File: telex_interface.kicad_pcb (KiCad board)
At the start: 4 copper layers, 61 x 34.5 mm, 14 parts, among them J1 DB25_Female_MountingHoles, J2 Conn_01x08, U1 max3387

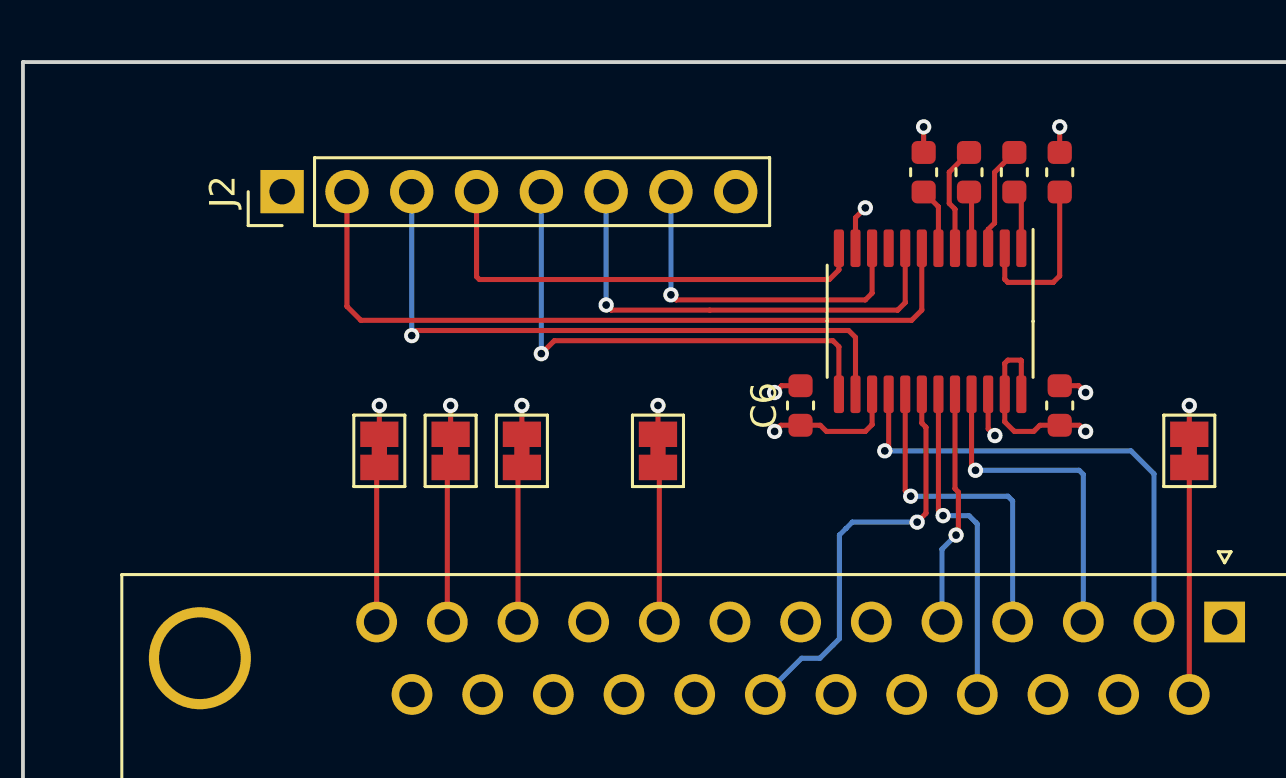
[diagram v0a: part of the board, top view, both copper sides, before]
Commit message: NAND gate for half dumplex echo and pullups
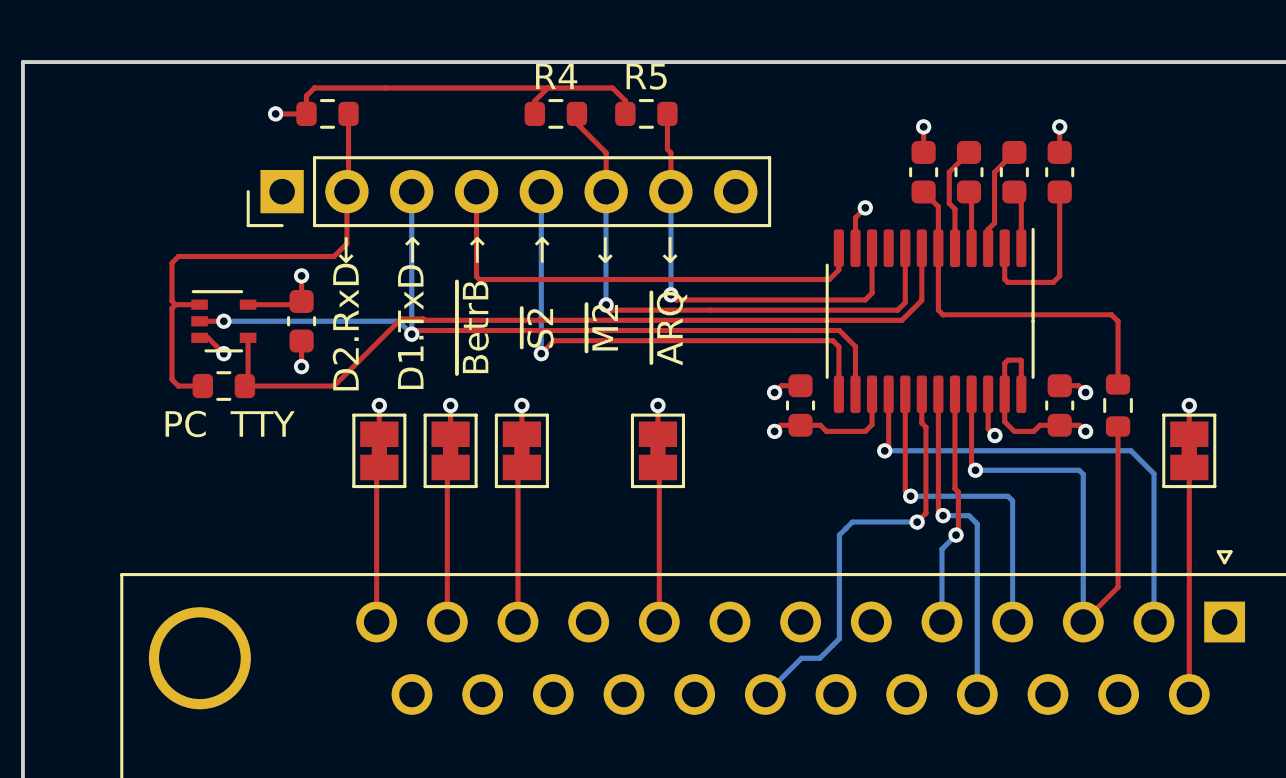
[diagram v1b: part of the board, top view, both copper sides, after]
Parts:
- added C7: 100n, Capacitor_SMD:C_0603_1608Metric, F.Cu at (158.2, 106.7)
- added R1: 3k6, Resistor_SMD:R_0603_1608Metric, F.Cu at (190.2, 110.0)
- added R2: 3k6, Resistor_SMD:R_0603_1608Metric, F.Cu at (159.3, 98.6)
- added R3: 0R (dnp), Resistor_SMD:R_0603_1608Metric, F.Cu at (155.2, 109.2)
- added R4: 3k6, Resistor_SMD:R_0603_1608Metric, F.Cu at (168.2, 98.6)
- added R5: 3k6, Resistor_SMD:R_0603_1608Metric, F.Cu at (171.8, 98.6)
- added U2: 74LVC1G08, Package_TO_SOT_SMD:SOT-353_SC-70-5, F.Cu at (155.2, 106.7)
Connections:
- net Net-(U1-Pad2) renamed +6V
- net Net-(U1-Pad6) renamed -6V
- J2 pad 2: /RxD -> /RxD_PC
- U1 pad 7: /RxD -> /RxD_TTY
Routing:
- net /RxD_TTY: track 0.00 -> 32.0 mm
- net /RxD: track 29.8 -> 0.00 mm
- net VCC: track 14.9 -> 34.6 mm, vias 3 -> 5
- net /RxD_PC: track 0.00 -> 19.2 mm
- net -6V: track 2.44 -> 14.6 mm
- net /TxD: track 25.5 -> 33.7 mm, vias 1 -> 2
- net V10_D2_RxD: track 13.1 -> 21.3 mm
- net /~{CTS}: track 18.5 -> 22.0 mm
- net /~{ARQ}: track 13.9 -> 17.0 mm
- net GND: track 11.6 -> 13.8 mm, vias 10 -> 12
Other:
- board text added: "D1.TxD"
- board text added: "D2.RxD"
- board text added: "PC"
- board text added: "TTY"
- board text added: "~{ARQ}"
- board text added: "~{BetrB}"
- board text added: "~{M2}"
- board text added: "~{S2}"
- board text added: "→"

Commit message: more work
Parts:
- removed R4, R5: 3k6, Resistor_SMD:R_0603_1608Metric
- added C10: 100n, Capacitor_SMD:C_0603_1608Metric, F.Cu at (206.0, 104.4)
- added C8: 10u, Capacitor_SMD:C_0603_1608Metric, F.Cu at (195.3, 98.6)
- added C9: 100n, Capacitor_SMD:C_0603_1608Metric, F.Cu at (194.6, 107.4)
- added J3: USB_B_Mini, Connector_USB:USB_Mini-B_Wuerth_65100516121_Horizontal, F.Cu at (203.2, 94.0)
- added JP6: Jumper_2_Open, Connector_PinHeader_2.54mm:PinHeader_2x01_P2.54mm_Vertical, F.Cu at (152.4, 113.0)
- added R6: 10k, Resistor_SMD:R_0603_1608Metric, F.Cu at (152.1, 108.7)
- added R7: 22R, Resistor_SMD:R_0603_1608Metric, F.Cu at (197.4, 98.6)
- added U3: CH340G, Package_SO:SOIC-16_3.9x9.9mm_P1.27mm, F.Cu at (200.7, 108.0)
- J2: value Conn_01x08 -> Conn_02x08_Odd_Even; footprint Connector_PinHeader_2.54mm:PinHeader_1x08_P2.54mm_Vertical -> Connector_PinHeader_2.54mm:PinHeader_2x08_P2.54mm_Vertical
- moved J2 19.3 mm to (175.3, 94.0), turned to -90 degrees
- moved R2 6.91 mm to (155.2, 104.1), turned to 180 degrees
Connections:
- net V10_M2_CTS renamed V10_M2
- J2 pad 1: VCC -> GND
- J2 pad 2: /RxD_PC -> VCC
- J2 pad 3: /TxD -> /USB_TxD
- J2 pad 4: /~{DTR} -> /RxD_PC
- J2 pad 5: /~{RTS} -> /USB_RxD
- J2 pad 6: /~{CTS} -> /TxD
- J2 pad 7: /~{ARQ} -> /~{USB_CTS}
- J2 pad 8: GND -> /~{S2_RTS}
- U1 pad 12: /~{DTR} -> /~{BetrB_DTR}
- U1 pad 13: /~{RTS} -> /~{S2_RTS}
- U1 pad 8: /~{CTS} -> /~{M2}
- U2 pad 2: /TxD -> Net-(JP6-Pad1)
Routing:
- net /~{USB_RTS}: track 0.00 -> 66.6 mm
- net /~{USB_DTR}: track 0.00 -> 64.3 mm
- net /~{USB_DCD}: track 0.00 -> 62.3 mm
- net /~{USB_DSR}: track 0.00 -> 61.5 mm
- net /~{USB_CTS}: track 0.00 -> 59.8 mm
- net /USB_TxD: track 0.00 -> 49.0 mm, vias 0 -> 1
- net /USB_RxD: track 0.00 -> 45.5 mm
- net /~{M2}: track 0.00 -> 29.4 mm, vias 0 -> 1
- net /~{S2_RTS}: track 0.00 -> 25.2 mm, vias 0 -> 1
- net /~{CTS}: track 22.0 -> 0.00 mm, vias 1 -> 0
- net /~{BetrB_DTR}: track 0.00 -> 20.8 mm
- net Net-(J3-Pad2): track 0.00 -> 20.4 mm, vias 0 -> 2
- net /~{RTS}: track 20.2 -> 0.00 mm, vias 1 -> 0
- net Net-(J3-Pad3): track 0.00 -> 19.6 mm, vias 0 -> 2
- net /~{DTR}: track 18.6 -> 0.00 mm
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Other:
- board size 61 x 34.5 mm -> 61 x 44.7 mm
- board text added: "CH340 FS200 Interface"
- board text added: "E21 #14"
- board text added: "E21 #9"
- board text added: "E22 #11"
- board text added: "E22 #12"
- board text added: "E22 #13"
- board text added: "RxD"
- board text added: "TxD"
- board text added: "USB"
- board text added: "Vcc"
- board text added: "bypass"
- board text added: "echo off"
- board text added: "~{CTS}"
- board text added: "~{DCD}"
- board text added: "~{DSR}"
- board text added: "~{DTR}"
- board text added: "~{RTS}"
- board text added: "⏚"
- board text removed: "PC"

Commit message: add power led
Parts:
- added D1: LED, LED_SMD:LED_0603_1608Metric, F.Cu at (182.1, 91.7)
- added R4: 22R, Resistor_SMD:R_0603_1608Metric, F.Cu at (186.1, 91.7)
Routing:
- net Net-(D1-Pad2): track 0.00 -> 2.40 mm
- net VCC: track 23.9 -> 24.9 mm, vias 5 -> 6
- net GND: track 28.4 -> 29.4 mm, vias 21 -> 22
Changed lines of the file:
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@@
   (net 56 "/~{USB_DTR}")
   (net 57 "/~{BetrB_DTR}")
+  (net 58 "Net-(D1-Pad2)")
   (footprint "Capacitor_SMD:C_0603_1608Metric" (layer "F.Cu")
     (at 182.626 100.838 90)
@@
       (net 36 "/RxD_TTY") (pintype "passive"))
     (model "${KICAD6_3DMODEL_DIR}/Resistor_SMD.3dshapes/R_0603_1608Metric.wrl"
+      (offset (xyz 0 0 0))
+      (scale (xyz 1 1 1))
+      (rotate (xyz 0 0 0))
+    )
+  )
+  (footprint "LED_SMD:LED_0603_1608Metric" (layer "F.Cu")
+    (at 182.118 91.694)
+    (descr "LED SMD 0603 (1608 Metric), square (rectangular) end terminal, IPC_7351 nominal, (Body size source: http://www.tortai-tech.com/upload/download/2011102023233369053.pdf), generated with kicad-footprint-generator")
+    (tags "LED")
+    (property "Sheetfile" "telex_interface.kicad_sch")
+    (property "Sheetname" "")
+    (attr smd)
+    (fp_text reference "D1" (at 0 -1.43) (layer "F.SilkS") hide
+      (effects (font (size 1 1) (thickness 0.15)))
+    )
+    (fp_text value "LED" (at 0 1.43) (layer "F.Fab") hide
+      (effects (font (size 1 1) (thickness 0.15)))
+    )
+    (fp_text user "${REFERENCE}" (at 0 0) (layer "F.Fab") hide
+      (effects (font (size 0.4 0.4) (thickness 0.06)))
+    )
+    (fp_line (start -1.485 0.735) (end 0.8 0.735) (layer "F.SilkS") (width 0.12))
+    (fp_line (start -1.485 -0.735) (end -1.485 0.735) (layer "F.SilkS") (width 0.12))
+    (fp_line (start 0.8 -0.735) (end -1.485 -0.735) (layer "F.SilkS") (width 0.12))
+    (fp_line (start -1.48 -0.73) (end 1.48 -0.73) (layer "F.CrtYd") (width 0.05))
+    (fp_line (start -1.48 0.73) (end -1.48 -0.73) (layer "F.CrtYd") (width 0.05))
+    (fp_line (start 1.48 0.73) (end -1.48 0.73) (layer "F.CrtYd") (width 0.05))
+    (fp_line (start 1.48 -0.73) (end 1.48 0.73) (layer "F.CrtYd") (width 0.05))
+    (fp_line (start -0.5 -0.4) (end -0.8 -0.1) (layer "F.Fab") (width 0.1))
+    (fp_line (start -0.8 -0.1) (end -0.8 0.4) (layer "F.Fab") (width 0.1))
+    (fp_line (start -0.8 0.4) (end 0.8 0.4) (layer "F.Fab") (width 0.1))
+    (fp_line (start 0.8 -0.4) (end -0.5 -0.4) (layer "F.Fab") (width 0.1))
+    (fp_line (start 0.8 0.4) (end 0.8 -0.4) (layer "F.Fab") (width 0.1))
+    (pad "1" smd roundrect locked (at -0.7875 0) (size 0.875 0.95) (layers "F.Cu" "F.Paste" "F.Mask") (roundrect_rratio 0.25)
+      (net 7 "GND") (pinfunction "K") (pintype "passive"))
+    (pad "2" smd roundrect locked (at 0.7875 0) (size 0.875 0.95) (layers "F.Cu" "F.Paste" "F.Mask") (roundrect_rratio 0.25)
+      (net 58 "Net-(D1-Pad2)") (pinfunction "A") (pintype "passive"))
+    (model "${KICAD6_3DMODEL_DIR}/LED_SMD.3dshapes/LED_0603_1608Metric.wrl"
       (offset (xyz 0 0 0))
       (scale (xyz 1 1 1))
@@
       (net 7 "GND") (pinfunction "Shield") (pintype "passive"))
     (model "${KICAD6_3DMODEL_DIR}/Connector_USB.3dshapes/USB_Mini-B_Wuerth_65100516121_Horizontal.wrl"
+      (offset (xyz 0 0 0))
+      (scale (xyz 1 1 1))
+      (rotate (xyz 0 0 0))
+    )
+  )
+  (footprint "Resistor_SMD:R_0603_1608Metric" (layer "F.Cu")
+    (at 186.128 91.694)
+    (descr "Resistor SMD 0603 (1608 Metric), square (rectangular) end terminal, IPC_7351 nominal, (Body size source: IPC-SM-782 page 72, https://www.pcb-3d.com/wordpress/wp-content/uploads/ipc-sm-782a_amendment_1_and_2.pdf), generated with kicad-footprint-generator")
+    (tags "resistor")
+    (property "Sheetfile" "telex_interface.kicad_sch")
+    (property "Sheetname" "")
+    (attr smd)
+    (fp_text reference "R4" (at 0 -1.43) (layer "F.SilkS") hide
+      (effects (font (size 1 1) (thickness 0.15)))
+    )
+    (fp_text value "22R" (at 0 1.43) (layer "F.Fab") hide
+      (effects (font (size 1 1) (thickness 0.15)))
+    )
+    (fp_text user "${REFERENCE}" (at 0 0) (layer "F.Fab") hide
+      (effects (font (size 0.4 0.4) (thickness 0.06)))
+    )
+    (fp_line (start -0.237258 0.5225) (end 0.237258 0.5225) (layer "F.SilkS") (width 0.12))
+    (fp_line (start -0.237258 -0.5225) (end 0.237258 -0.5225) (layer "F.SilkS") (width 0.12))
+    (fp_line (start 1.48 -0.73) (end 1.48 0.73) (layer "F.CrtYd") (width 0.05))
+    (fp_line (start -1.48 -0.73) (end 1.48 -0.73) (layer "F.CrtYd") (width 0.05))
+    (fp_line (start 1.48 0.73) (end -1.48 0.73) (layer "F.CrtYd") (width 0.05))
+    (fp_line (start -1.48 0.73) (end -1.48 -0.73) (layer "F.CrtYd") (width 0.05))
+    (fp_line (start -0.8 0.4125) (end -0.8 -0.4125) (layer "F.Fab") (width 0.1))
+    (fp_line (start 0.8 0.4125) (end -0.8 0.4125) (layer "F.Fab") (width 0.1))
+    (fp_line (start 0.8 -0.4125) (end 0.8 0.4125) (layer "F.Fab") (width 0.1))
+    (fp_line (start -0.8 -0.4125) (end 0.8 -0.4125) (layer "F.Fab") (width 0.1))
+    (pad "1" smd roundrect locked (at -0.825 0) (size 0.8 0.95) (layers "F.Cu" "F.Paste" "F.Mask") (roundrect_rratio 0.25)
+      (net 58 "Net-(D1-Pad2)") (pintype "passive"))
+    (pad "2" smd roundrect locked (at 0.825 0) (size 0.8 0.95) (layers "F.Cu" "F.Paste" "F.Mask") (roundrect_rratio 0.25)
+      (net 2 "VCC") (pintype "passive"))
+    (model "${KICAD6_3DMODEL_DIR}/Resistor_SMD.3dshapes/R_0603_1608Metric.wrl"
       (offset (xyz 0 0 0))
       (scale (xyz 1 1 1))
@@
   (segment (start 180.605 110.733) (end 180.34 110.998) (width 0.2) (layer "F.Cu") (net 2))
   (segment (start 177.8 110.757) (end 177.025 110.757) (width 0.2) (layer "F.Cu") (net 2))
+  (segment (start 186.953 91.694) (end 187.96 91.694) (width 0.2) (layer "F.Cu") (net 2))
   (segment (start 156.144 104.265) (end 156.019 104.14) (width 0.2) (layer "F.Cu") (net 2))
   (segment (start 179.955 103.8175) (end 179.955 102.62) (width 0.2) (layer "F.Cu") (net 2))
@@
   (via (at 180.34 102.235) (size 0.6) (drill 0.3) (layers "F.Cu" "B.Cu") (net 2))
   (via (at 176.784 110.998) (size 0.6) (drill 0.3) (layers "F.Cu" "B.Cu") (net 2))
+  (via (at 187.96 91.694) (size 0.6) (drill 0.3) (layers "F.Cu" "B.Cu") (net 2))
   (via (at 158.242 104.902) (size 0.6) (drill 0.3) (layers "F.Cu" "B.Cu") (net 2))
   (via (at 188.976 110.998) (size 0.6) (drill 0.3) (layers "F.Cu" "B.Cu") (net 2))
@@
   (segment (start 204.298 89.58) (end 204.216 89.662) (width 0.2) (layer "F.Cu") (net 7))
   (segment (start 161.29 111.11) (end 161.29 109.982) (width 0.2) (layer "F.Cu") (net 7))
+  (segment (start 181.3305 91.694) (end 180.34 91.694) (width 0.2) (layer "F.Cu") (net 7))
   (segment (start 185.155 109.5425) (end 185.155 110.8955) (width 0.2) (layer "F.Cu") (net 7))
   (segment (start 200.6 89.58) (end 198.71 89.58) (width 0.2) (layer "F.Cu") (net 7))
@@
   (via (at 158.242 108.458) (size 0.6) (drill 0.3) (layers "F.Cu" "B.Cu") (net 7))
   (via (at 182.626 99.06) (size 0.6) (drill 0.3) (layers "F.Cu" "B.Cu") (net 7))
+  (via (at 180.34 91.694) (size 0.6) (drill 0.3) (layers "F.Cu" "B.Cu") (net 7))
   (via (at 166.878 109.982) (size 0.6) (drill 0.3) (layers "F.Cu" "B.Cu") (net 7))
   (segment (start 172.265 118.469669) (end 172.265 112.463) (width 0.2) (layer "F.Cu") (net 9))
@@
   (segment (start 178.308 99.06) (end 165.354 99.06) (width 0.2) (layer "F.Cu") (net 57))
   (segment (start 165.354 99.06) (end 165.1 98.806) (width 0.2) (layer "F.Cu") (net 57))
+  (segment (start 182.9055 91.694) (end 185.303 91.694) (width 0.2) (layer "F.Cu") (net 58))
   (zone locked (net 7) (net_name "GND") (layer "In1.Cu") (hatch edge 0.508)
     (connect_pads (clearance 0.3))

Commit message: more work
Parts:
- added C11: 22p, Capacitor_SMD:C_0603_1608Metric, F.Cu at (188.7, 97.0)
- added C12: 22p, Capacitor_SMD:C_0603_1608Metric, F.Cu at (190.8, 97.0)
- added H1: MountingHole_Pad, MountingHole:MountingHole_3.2mm_M3_DIN965_Pad, F.Cu at (203.2, 111.8)
- added H2: MountingHole_Pad, MountingHole:MountingHole_3.2mm_M3_DIN965_Pad, F.Cu at (152.4, 91.4)
- added JP7: SolderJumper_2_Bridged, Jumper:SolderJumper-2_P1.3mm_Bridged_Pad1.0x1.5mm, F.Cu at (195.8, 111.8)
- added TP1: TestPoint, TestPoint:TestPoint_Pad_2.0x2.0mm, B.Cu at (190.8, 125.0)
- added TP10: TestPoint, TestPoint:TestPoint_Pad_2.0x2.0mm, B.Cu at (197.4, 125.0)
- added TP11: TestPoint, TestPoint:TestPoint_Pad_2.0x2.0mm, B.Cu at (192.3, 104.4)
- added TP12: TestPoint, TestPoint:TestPoint_Pad_2.0x2.0mm, F.Cu at (149.9, 99.8)
- added TP13: TestPoint, TestPoint:TestPoint_Pad_2.0x2.0mm, F.Cu at (149.9, 103.1)
- added TP2: TestPoint, TestPoint:TestPoint_Pad_2.0x2.0mm, B.Cu at (180.8, 125.0)
- added TP3: TestPoint, TestPoint:TestPoint_Pad_2.0x2.0mm, B.Cu at (184.2, 125.0)
- added TP4: TestPoint, TestPoint:TestPoint_Pad_2.0x2.0mm, B.Cu at (194.1, 125.0)
- added TP5: TestPoint, TestPoint:TestPoint_Pad_2.0x2.0mm, B.Cu at (187.5, 125.0)
- added TP6: TestPoint, TestPoint:TestPoint_Pad_2.0x2.0mm, B.Cu at (177.5, 125.0)
- added TP7: TestPoint, TestPoint:TestPoint_Pad_2.0x2.0mm, B.Cu at (189.0, 104.4)
- added TP8: TestPoint, TestPoint:TestPoint_Pad_2.0x2.0mm, B.Cu at (189.0, 107.7)
- added TP9: TestPoint, TestPoint:TestPoint_Pad_2.0x2.0mm, B.Cu at (192.3, 107.7)
- added Y1: EuroQuartz MJ 5x3.2mm 12MHz, Crystal:Crystal_SMD_EuroQuartz_MJ-4Pin_5.0x3.2mm_HandSoldering, F.Cu at (194.8, 91.4)
- moved C10 31.4 mm to (178.8, 88.6), turned to 0 degrees
- moved D1 25.6 mm to (205.3, 102.6), turned to 180 degrees
- moved U3 22.2 mm to (186.2, 91.2), turned to 90 degrees
- moved R4 18.7 mm to (201.2, 102.6), turned to 180 degrees
- moved C9 15.5 mm to (184.2, 96.0)
- moved C8 1.80 mm to (193.5, 98.3), turned to 90 degrees
- moved R7 1.44 mm to (196.3, 97.5), turned to 180 degrees
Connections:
- net Net-(J3-Pad2) renamed /USB_DN
- net Net-(J3-Pad3) renamed /USB_DP
- J1 pad 1: unconnected-(J1-Pad1) -> /SHIELD@1
- U3 pad 7: unconnected-(U3-Pad7) -> Net-(U3-Pad7)
- U3 pad 8: unconnected-(U3-Pad8) -> Net-(U3-Pad8)
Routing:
- net /USB_TxD: track 49.0 -> 12.0 mm, vias 1 -> 0
- net /~{USB_RTS}: track 66.6 -> 31.7 mm
- net /~{USB_DTR}: track 64.3 -> 30.3 mm
- net /~{USB_DCD}: track 62.3 -> 29.2 mm
- net /~{USB_DSR}: track 61.5 -> 29.2 mm
- net /~{USB_CTS}: track 59.8 -> 27.8 mm
- net /USB_RxD: track 45.5 -> 17.2 mm
- net GND: track 29.4 -> 41.5 mm, vias 22 -> 30
- net Net-(U3-Pad8): track 0.00 -> 11.3 mm
- net Net-(U3-Pad7): track 0.00 -> 9.85 mm
- net V10_D1_TxD: track 19.0 -> 27.4 mm
- net V10_M2: track 9.25 -> 17.6 mm
- net V10_D2_RxD: track 21.3 -> 29.1 mm
- net V10_S2_RTS: track 12.9 -> 20.4 mm
- net VBUS: track 17.4 -> 24.6 mm, vias 0 -> 2
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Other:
- outline, holes or cut-outs redrawn
- board text added: "+6V"
- board text added: "-6V"
- board text added: "ARQ"
- board text added: "BetrB DTR"
- board text added: "D1 TxD"
- board text added: "D2 RxD"
- board text added: "M2"
- board text added: "S2 RTS"
- board text added: "SHLD #1"
- board text added: "USB_DN"
- board text added: "USB_DP"
- board text added: "VBUS"

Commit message: Add Raspi header.
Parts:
- added J4: Raspberry_Pi_2_3, Connector_PinSocket_2.54mm:PinSocket_2x20_P2.54mm_Vertical, B.Cu at (149.9, 83.8)
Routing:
- net /~{BetrB_DTR}: track 20.8 -> 42.3 mm, vias 0 -> 1
- net /TxD: track 45.8 -> 64.9 mm
- net /RxD_PC: track 36.2 -> 52.6 mm
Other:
- board size 61 x 44.7 mm -> 61 x 52.3 mm
- board text added: "GPIOs: 27=D1 17=D2 10=BetrB"
